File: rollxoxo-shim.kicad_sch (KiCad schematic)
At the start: 56 parts, among them J1 Conn_01x10, J2 USB_C_Receptacle_USB2.0_14P, J3 Conn_01x02, J4 Conn_01x04_Pin, SW1 SW_Push, SW2 SW_Push, U1 SN74LV1T125DBV, U2 ESP32-S3FN8, U3 SN74LV1T125DBV, U4 SN74LV1T125DBV, Y1 48M

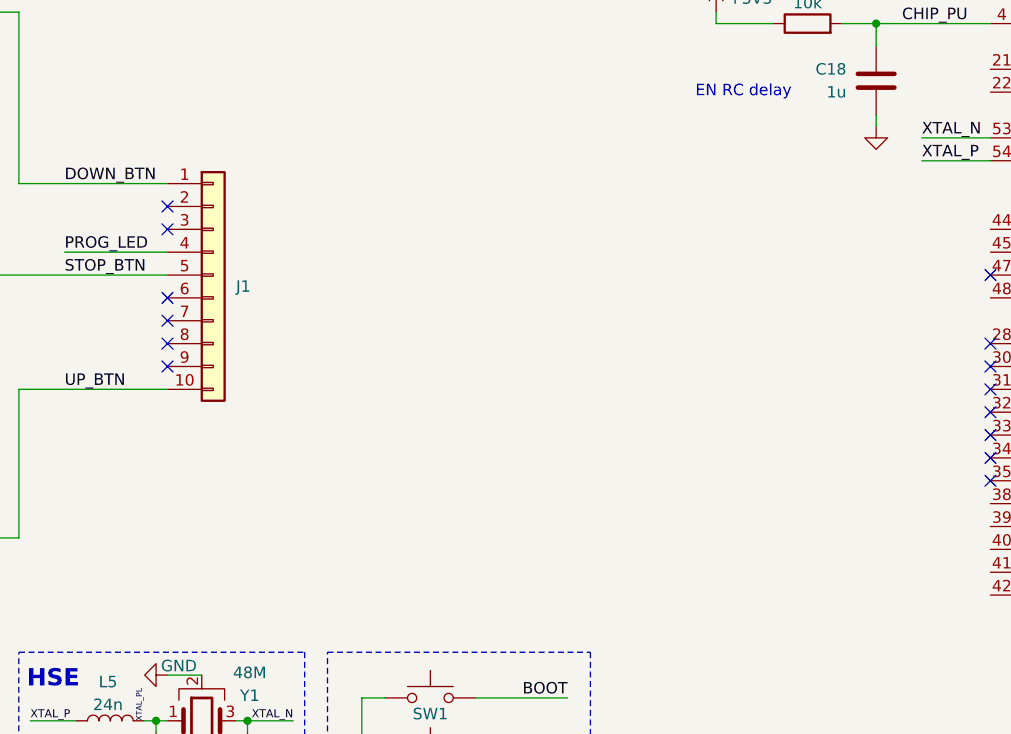
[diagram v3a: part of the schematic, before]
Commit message: schem: add LIGHT level shifter
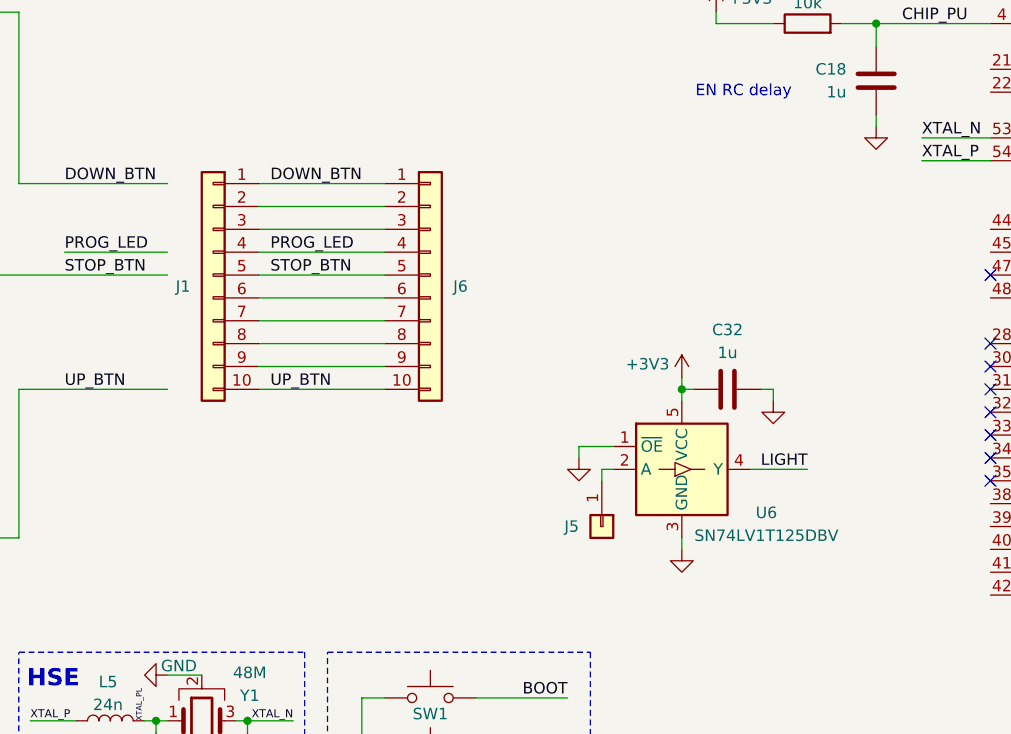
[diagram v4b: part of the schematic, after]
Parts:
- added C32: 1u, Capacitor_SMD:C_0402_1005Metric, symbol Device:C
- added J5: Conn_01x01, Connector_PinHeader_2.54mm:PinHeader_1x01_P2.54mm_Horizontal, symbol Connector_Generic:Conn_01x01
- added J6: Conn_01x10, Connector_PinHeader_2.54mm:PinHeader_1x10_P2.54mm_Horizontal, symbol Connector_Generic:Conn_01x10
- added U6: SN74LV1T125DBV, Package_TO_SOT_SMD:SOT-23-5, symbol Logic_LevelTranslator:SN74LV1T125DBV
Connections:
- net +3V3: now also C32.1, U6.5 (VCC)
- net DOWN_BTN: now also J6.1 (Pin_1)
- net GND: now also C32.2, U6.1 (~{OE}), U6.3 (GND)
- net PROG_LED: now also J6.4 (Pin_4)
- net STOP_BTN: now also J6.5 (Pin_5)
- net UP_BTN: now also J6.10 (Pin_10)
- net at J1.2 (Pin_2): now also J6.2 (Pin_2)
- net at J1.3 (Pin_3): now also J6.3 (Pin_3)
- net at J1.6 (Pin_6): now also J6.6 (Pin_6)
- net at J1.7 (Pin_7): now also J6.7 (Pin_7)
- net at J1.8 (Pin_8): now also J6.8 (Pin_8)
- net at J1.9 (Pin_9): now also J6.9 (Pin_9)
- new net: J5.1 (Pin_1), U6.2 (A)
- new net LIGHT: U6.4 (Y)
- no-connect marks 19 -> 13
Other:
- moved on the sheet: J1

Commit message: schem: reorganize
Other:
- note added: "BUTTONS LEVEL SHIFTERS"
- note added: "LIGHT SHIFTER"
- note added: "SHIM HEADERS"
- moved on the sheet: AE1, C16, C17, C18, C19, C20, C21, C22, C24, C26, C27, C28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

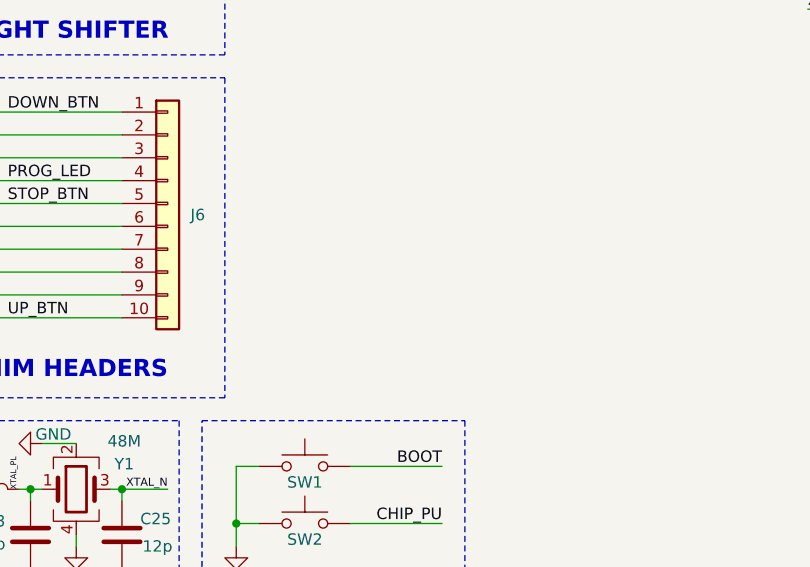
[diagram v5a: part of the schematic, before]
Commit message: schem: add reed switches header
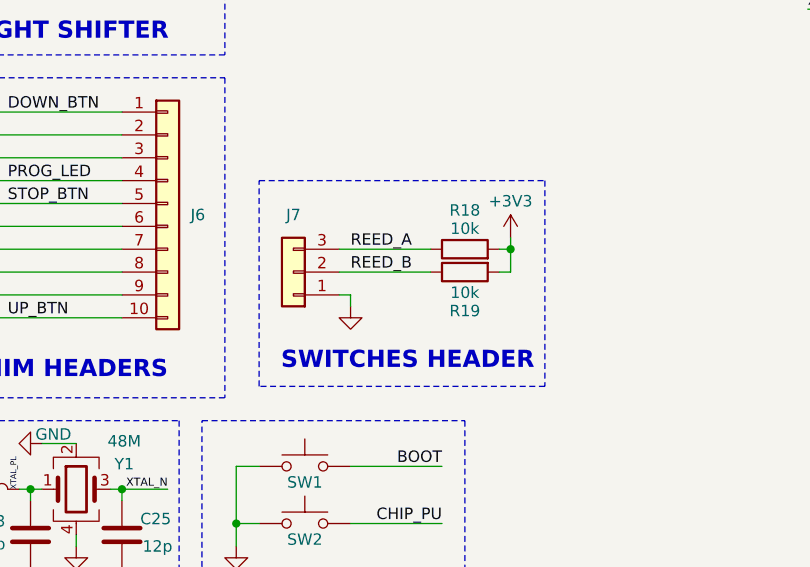
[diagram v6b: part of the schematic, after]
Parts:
- added J7: Conn_01x03, symbol Connector_Generic:Conn_01x03
- added R18, R19: 10k, Resistor_SMD:R_0402_1005Metric, symbol Device:R
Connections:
- net +3V3: now also R18.2, R19.2
- net GND: now also J7.1 (Pin_1)
- new net REED_A: J7.3 (Pin_3), R18.1
- new net REED_B: J7.2 (Pin_2), R19.1
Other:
- note added: "SWITCHES HEADER"

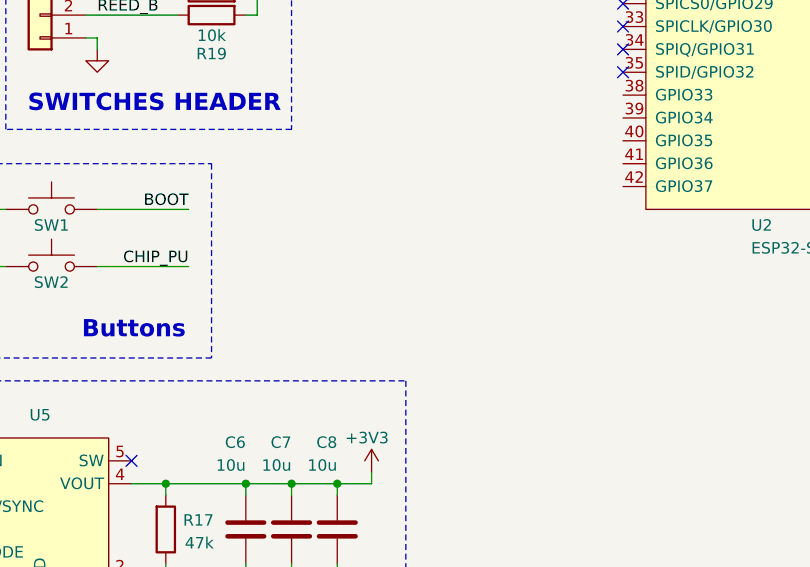
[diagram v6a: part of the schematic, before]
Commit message: schem: add flash voltage divider input
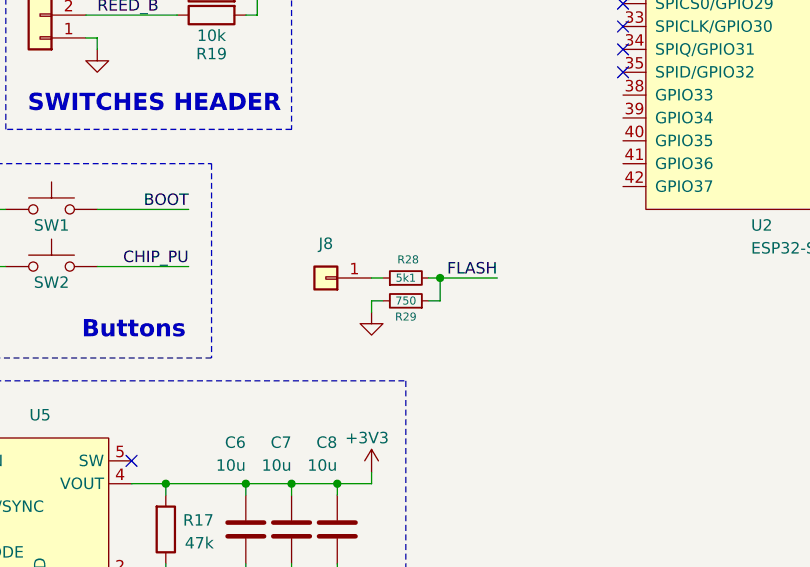
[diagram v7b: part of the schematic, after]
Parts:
- added J8: Conn_01x01, Connector_PinHeader_2.54mm:PinHeader_1x01_P2.54mm_Horizontal, symbol Connector_Generic:Conn_01x01
- added R28: 5k1, Resistor_SMD:R_0603_1608Metric, symbol Device:R_Small
- added R29: 750, Resistor_SMD:R_0603_1608Metric, symbol Device:R_Small
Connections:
- net GND: now also R29.2
- new net: J8.1 (Pin_1), R28.1
- new net FLASH: R28.2, R29.1

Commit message: schem: add test points
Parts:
- added TP4, TP5, TP6, TP7: TestPoint, TestPoint:TestPoint_Pad_D1.0mm, symbol Connector:TestPoint
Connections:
- net +3V3: now also TP4.1
- net FLASH: now also TP7.1
- net LIGHT: now also TP6.1
- net UP_BTN: now also TP5.1
